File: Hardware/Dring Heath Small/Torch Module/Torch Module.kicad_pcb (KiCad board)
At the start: 2 copper layers, 86.5 x 74.7 mm, 32 parts, among them J1 Torch, J2 Module3, J3 Conn_01x18_Male, J4 Limit, J6 Motor, J7 Module1, K1 G6E, Q1 AO3400A, U1 ULN2002

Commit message: Main and Module Boards Routed
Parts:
- removed C3: 1uf, Capacitor_SMD:C_0603_1608Metric_Pad1.08x0.95mm_HandSolder
- removed R10: 3.3k, Resistor_SMD:R_0603_1608Metric_Pad0.98x0.95mm_HandSolder
- removed R8: 10k, Resistor_SMD:R_0603_1608Metric_Pad0.98x0.95mm_HandSolder
- removed R9: 1k, Resistor_SMD:R_0603_1608Metric_Pad0.98x0.95mm_HandSolder
- added J10: ~, Connector_PinHeader_2.54mm:PinHeader_1x12_P2.54mm_Vertical, F.Cu at (175.2, 129.6)
- added J8: 2.54 pin, Connector_PinHeader_2.54mm:PinHeader_2x05_P2.54mm_Vertical, F.Cu at (182.2, 111.9)
- added J9: 1.27 pin, Connector_PinHeader_1.27mm:PinHeader_2x05_P1.27mm_Vertical, F.Cu at (181.7, 125.3)
- J2: value Module3 -> ~
- J3: value Conn_01x18_Male -> ~
- moved R13 7.90 mm to (146.8, 109.1)
- moved R14 7.90 mm to (146.8, 123.6)
- moved J4 7.90 mm to (153.9, 120.3)
- moved C4 7.90 mm to (142.5, 109.1)
- moved C5 7.90 mm to (142.7, 123.6)
- moved J7 7.90 mm to (127.0, 129.7)
- moved R11 7.90 mm to (147.8, 113.9)
- moved R12 7.90 mm to (147.8, 119.0)
- moved R15 7.90 mm to (143.3, 113.9)
- moved R16 7.90 mm to (143.3, 119.0)
- moved J3 1.27 mm to (106.0, 64.3)
- moved U1 1.27 mm to (106.0, 58.4)
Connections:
- J3 pad 17: Net-(C3-Pad2) -> (no net)
- J3 pad 18: Net-(C3-Pad2) -> Net-(J3-Pad18)
- J3 pad 9: Net-(J3-Pad9) -> Net-(J3-Pad15)
- U1 pad 13: Net-(U1-Pad13) -> Net-(J3-Pad11)
- U1 pad 4: Net-(C3-Pad1) -> Net-(J3-Pad4)
- U1 pad 5: Net-(C3-Pad1) -> Net-(J3-Pad15)
- U1 pad 6: Net-(C3-Pad1) -> Net-(J3-Pad15)
- U1 pad 7: Net-(C3-Pad1) -> Net-(J3-Pad15)
- U1 pad 8: Net-(C3-Pad1) -> Net-(J3-Pad15)
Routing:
- net Net-(J3-Pad15): track 0.00 -> 50.9 mm
- net Net-(J10-Pad1): track 0.00 -> 49.9 mm
- net Net-(C3-Pad1): track 35.9 -> 0.00 mm
- net Net-(J10-Pad11): track 0.00 -> 27.1 mm
- net Net-(J10-Pad3): track 0.00 -> 26.5 mm
- net Net-(J10-Pad10): track 0.00 -> 23.4 mm, vias 0 -> 1
- net Net-(J10-Pad9): track 0.00 -> 22.3 mm, vias 0 -> 1
- net Net-(J10-Pad8): track 0.00 -> 20.5 mm
- net Net-(J3-Pad4): track 0.00 -> 15.5 mm, vias 0 -> 1
- net Net-(R10-Pad2): track 13.1 -> 0.00 mm, vias 2 -> 0
- net Net-(C3-Pad2): track 10.4 -> 0.00 mm
- net Net-(J3-Pad11): track 10.8 -> 4.35 mm, vias 1 -> 0
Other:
- board size 86.5 x 74.7 mm -> 88.6 x 79.4 mm
- board text added: "Clearpath Driver"
- board text added: "GND"
- board text added: "JTAG"
- board text added: "TCK"
- board text added: "TDI"
- board text added: "TDO"
- board text added: "TMS"
- board text added: "VCC"
- board text removed: "Z AXIS"

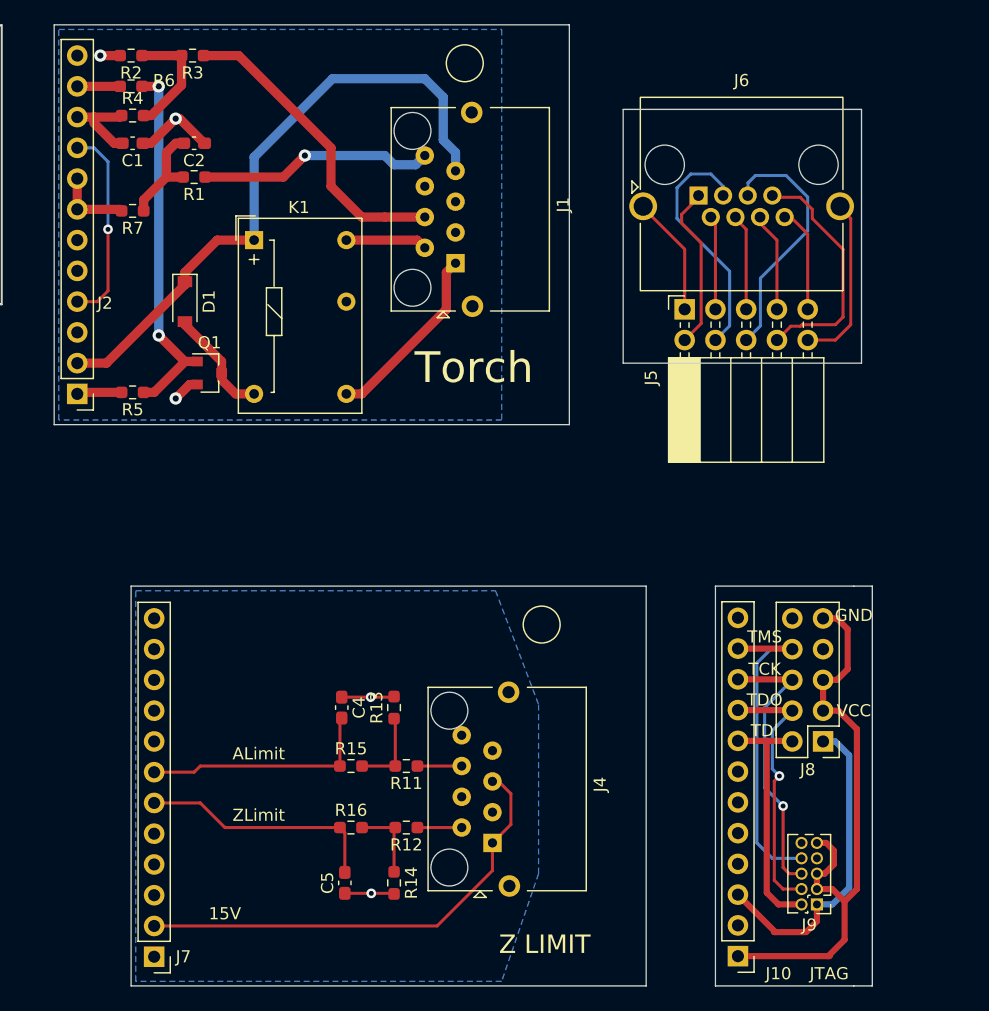
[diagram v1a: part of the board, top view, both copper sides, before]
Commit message: Pin changes
Put RJ45 connector on Jtag module for more IO put Pot on Torch module to
adjust Plasma voltage
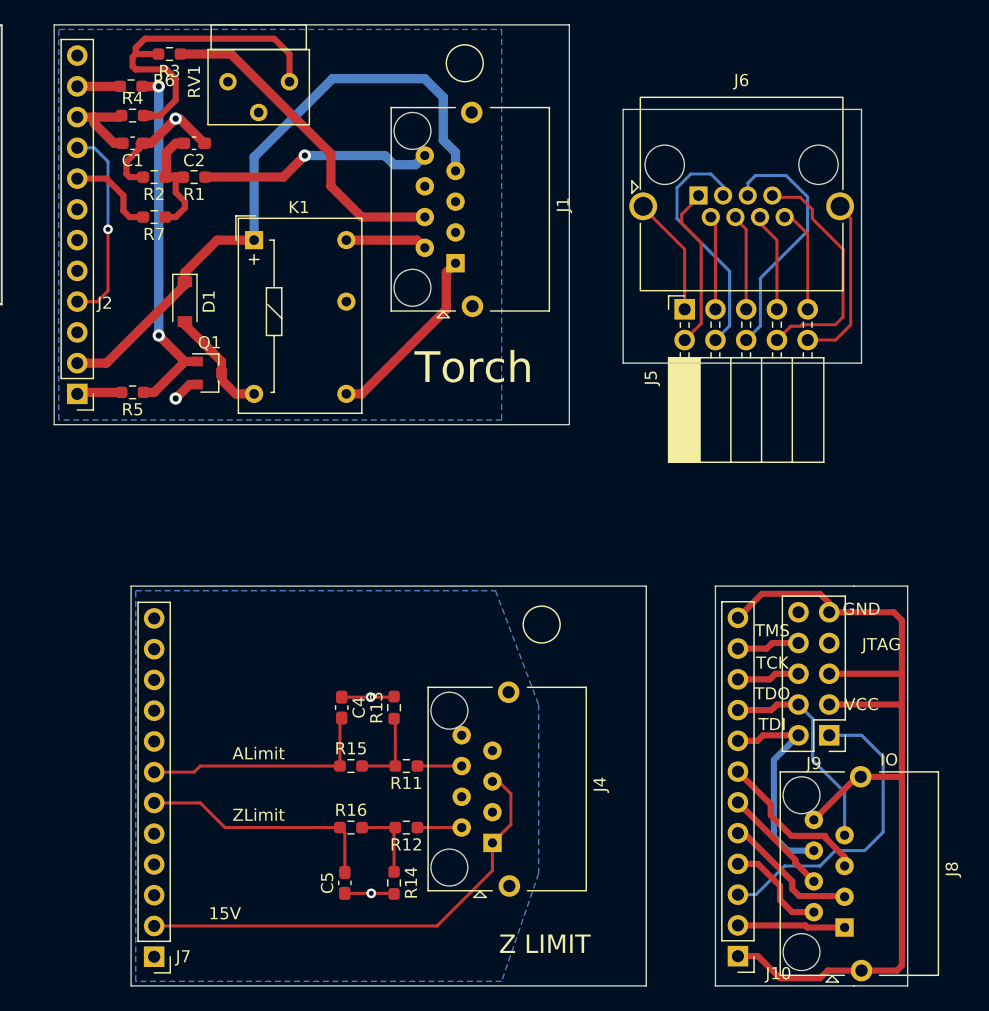
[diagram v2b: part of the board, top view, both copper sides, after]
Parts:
- added RV1: 20K, Potentiometer_THT:Potentiometer_Bourns_3339S_Horizontal, F.Cu at (133.1, 57.4)
- C2: value .1uf -> 1uf
- J2: value ~ -> Module3
- J3: value ~ -> Conn_01x18_Male
- J8: value 2.54 pin -> Torch; footprint Connector_PinHeader_2.54mm:PinHeader_2x05_P2.54mm_Vertical -> Modules:RJ45_Torb_Vertical
- J9: value 1.27 pin -> 2.54 pin; footprint Connector_PinHeader_1.27mm:PinHeader_2x05_P1.27mm_Vertical -> Connector_PinHeader_2.54mm:PinHeader_2x05_P2.54mm_Vertical
- R1: value 10k -> 3.3K
- moved J8 15.4 mm to (183.0, 127.3), turned to 90 degrees
- moved J9 14.0 mm to (182.8, 111.4)
- moved R2 10.2 mm to (127.0, 65.3)
- moved R3 1.91 mm to (128.3, 55.1)
- moved R7 1.85 mm to (127.0, 68.6)
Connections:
- J10 pad 12: Net-(J10-Pad12) -> Net-(J10-Pad1)
- J2 pad 8: Net-(J2-Pad7) -> Net-(J2-Pad8)
- J3 pad 17: (no net) -> Net-(J3-Pad17)
- J8 pad 1: Net-(J10-Pad3) -> Net-(J10-Pad2)
- J8 pad 10: Net-(J8-Pad10) -> Net-(J10-Pad1)
- J8 pad 2: Net-(J10-Pad8) -> Net-(J10-Pad4)
- J8 pad 3: Net-(J10-Pad1) -> Net-(J10-Pad5)
- J8 pad 4: Net-(J10-Pad9) -> Net-(J10-Pad6)
- J8 pad 5: Net-(J10-Pad1) -> Net-(J10-Pad7)
- J8 pad 6: Net-(J10-Pad10) -> Net-(J10-Pad8)
- J8 pad 7: Net-(J8-Pad7) -> Net-(J10-Pad9)
- J8 pad 8: Net-(J10-Pad11) -> Net-(J10-Pad1)
- R2 pad 1: Net-(R2-Pad1) -> Net-(C2-Pad2)
- R3 pad 2: Net-(R2-Pad1) -> Net-(R3-Pad2)
- R4 pad 2: Net-(R2-Pad1) -> Net-(R3-Pad2)
- R7 pad 2: Net-(J2-Pad7) -> Net-(J2-Pad8)
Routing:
- net Net-(J10-Pad1): track 49.9 -> 79.8 mm
- net Net-(R3-Pad2): track 0.00 -> 28.6 mm
- net Net-(J10-Pad11): track 27.1 -> 5.26 mm
- net Net-(J10-Pad10): track 23.4 -> 5.26 mm, vias 1 -> 0
- net Net-(J10-Pad7): track 0.00 -> 13.1 mm
- net Net-(J10-Pad5): track 0.00 -> 11.4 mm
- net Net-(R2-Pad1): track 10.8 -> 0.00 mm
- net Net-(J10-Pad6): track 0.00 -> 9.12 mm
- net Net-(J10-Pad2): track 0.00 -> 8.88 mm
- net Net-(J10-Pad4): track 0.00 -> 8.59 mm
- net Net-(J2-Pad8): track 0.00 -> 7.50 mm
- net Net-(J2-Pad7): track 6.25 -> 0.00 mm
- net Net-(J10-Pad9): track 22.3 -> 17.6 mm, vias 1 -> 0
- net Net-(C1-Pad1): track 14.4 -> 17.5 mm, vias 3 -> 2
- net Net-(J10-Pad8): track 20.5 -> 18.3 mm
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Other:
- board size 88.6 x 79.4 mm -> 91.6 x 79.4 mm
- board text added: "IO"

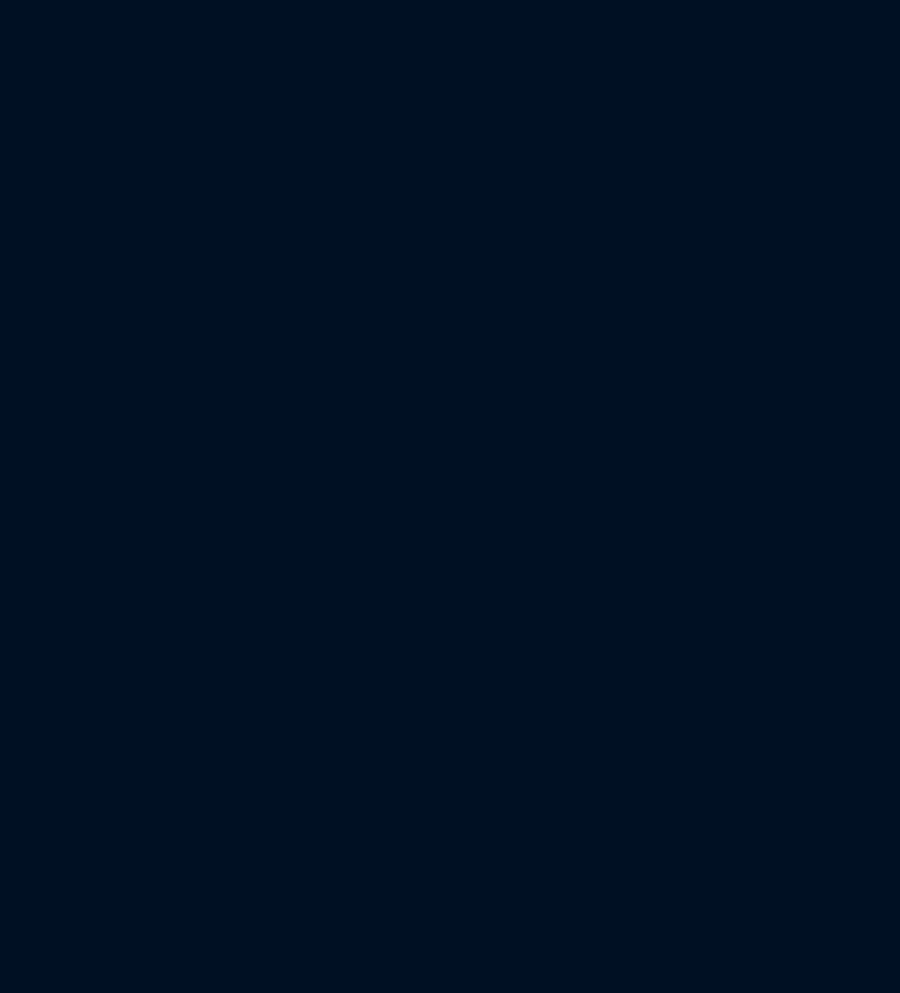
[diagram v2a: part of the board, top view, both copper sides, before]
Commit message: Added mosfet motor driver
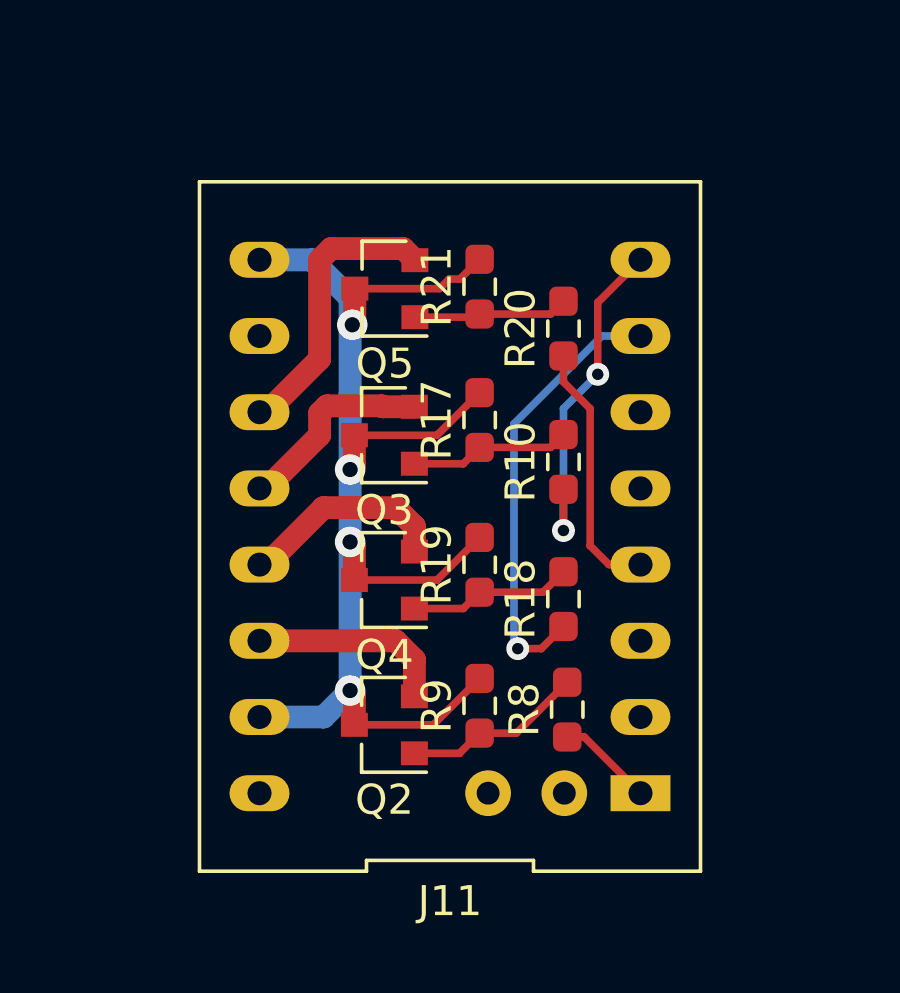
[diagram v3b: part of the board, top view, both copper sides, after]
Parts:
- added J11: Conn_01x18_Male, Modules:ClearpathDriver, F.Cu at (136.8, 150.0)
- added Q2: IRLML2402, Package_TO_SOT_SMD:SOT-23, F.Cu at (134.6, 156.6)
- added Q3: IRLML2402, Package_TO_SOT_SMD:SOT-23, F.Cu at (134.6, 146.9)
- added Q4: IRLML2402, Package_TO_SOT_SMD:SOT-23, F.Cu at (134.6, 151.8)
- added Q5: IRLML2402, Package_TO_SOT_SMD:SOT-23, F.Cu at (134.6, 142.1)
- added R10: 200, Resistor_SMD:R_0603_1608Metric_Pad0.98x0.95mm_HandSolder, F.Cu at (140.6, 147.8)
- added R17: 10k, Resistor_SMD:R_0603_1608Metric_Pad0.98x0.95mm_HandSolder, F.Cu at (137.8, 146.4)
- added R18: 200, Resistor_SMD:R_0603_1608Metric_Pad0.98x0.95mm_HandSolder, F.Cu at (140.6, 152.4)
- added R19: 10k, Resistor_SMD:R_0603_1608Metric_Pad0.98x0.95mm_HandSolder, F.Cu at (137.8, 151.3)
- added R20: 200, Resistor_SMD:R_0603_1608Metric_Pad0.98x0.95mm_HandSolder, F.Cu at (140.6, 143.4)
- added R21: 10k, Resistor_SMD:R_0603_1608Metric_Pad0.98x0.95mm_HandSolder, F.Cu at (137.8, 142.0)
- added R8: 200, Resistor_SMD:R_0603_1608Metric_Pad0.98x0.95mm_HandSolder, F.Cu at (140.7, 156.1)
- added R9: 10k, Resistor_SMD:R_0603_1608Metric_Pad0.98x0.95mm_HandSolder, F.Cu at (137.8, 156.0)
- J10: value ~ -> Module conn
- Q1: value AO3400A -> IRLML2402
- R6: value 10k -> 200
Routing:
- net Net-(J11-Pad15): track 0.00 -> 43.9 mm, vias 0 -> 4
- net Net-(J11-Pad7): track 0.00 -> 14.8 mm, vias 0 -> 1
- net Net-(J11-Pad8): track 0.00 -> 11.7 mm, vias 0 -> 2
- net Net-(J11-Pad11): track 0.00 -> 9.53 mm
- net Net-(J11-Pad4): track 0.00 -> 8.63 mm
- net Net-(J11-Pad13): track 0.00 -> 7.05 mm
- net Net-(J11-Pad12): track 0.00 -> 6.75 mm
- net Net-(J11-Pad14): track 0.00 -> 6.65 mm
- net Net-(Q2-Pad1): track 0.00 -> 6.08 mm
- net Net-(Q4-Pad1): track 0.00 -> 5.48 mm
- net Net-(Q3-Pad1): track 0.00 -> 5.37 mm
- net Net-(Q5-Pad1): track 0.00 -> 5.17 mm
- net Net-(J11-Pad1): track 0.00 -> 3.22 mm

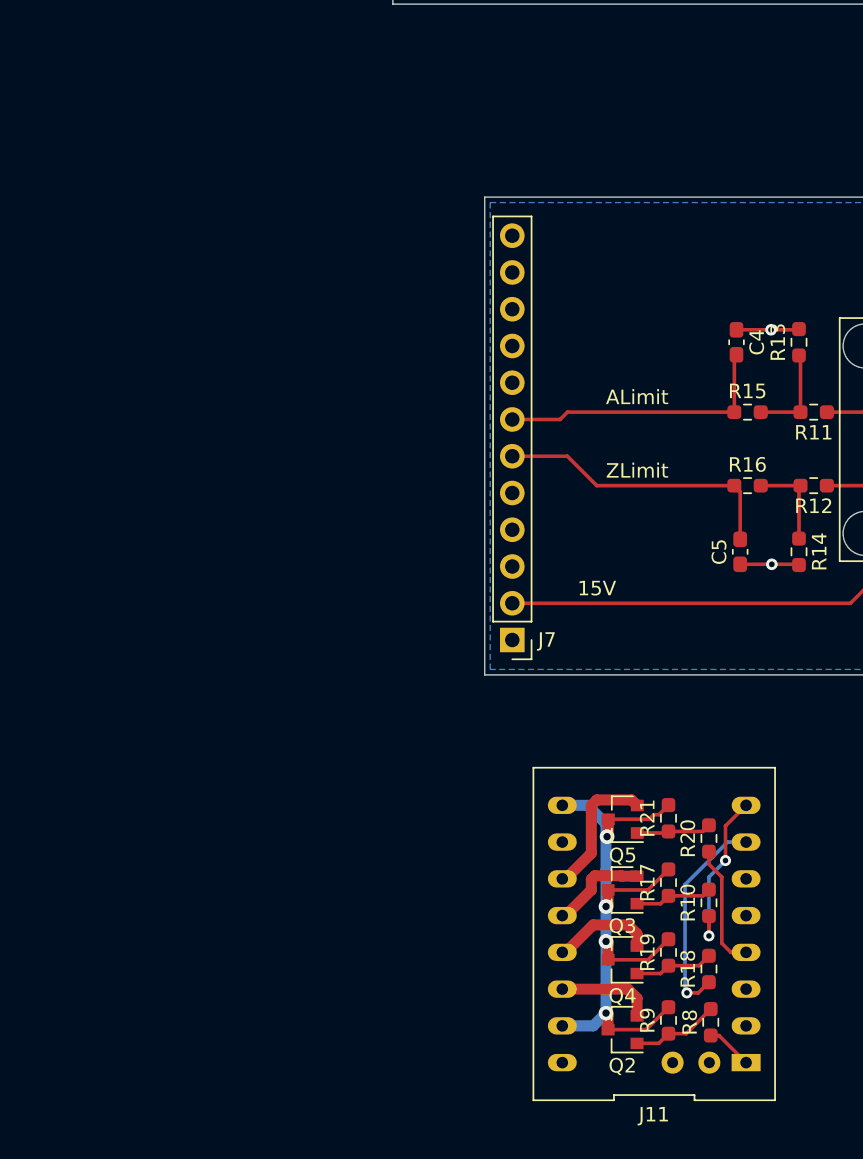
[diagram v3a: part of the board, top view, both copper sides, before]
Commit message: Changed voltage divider for THC input
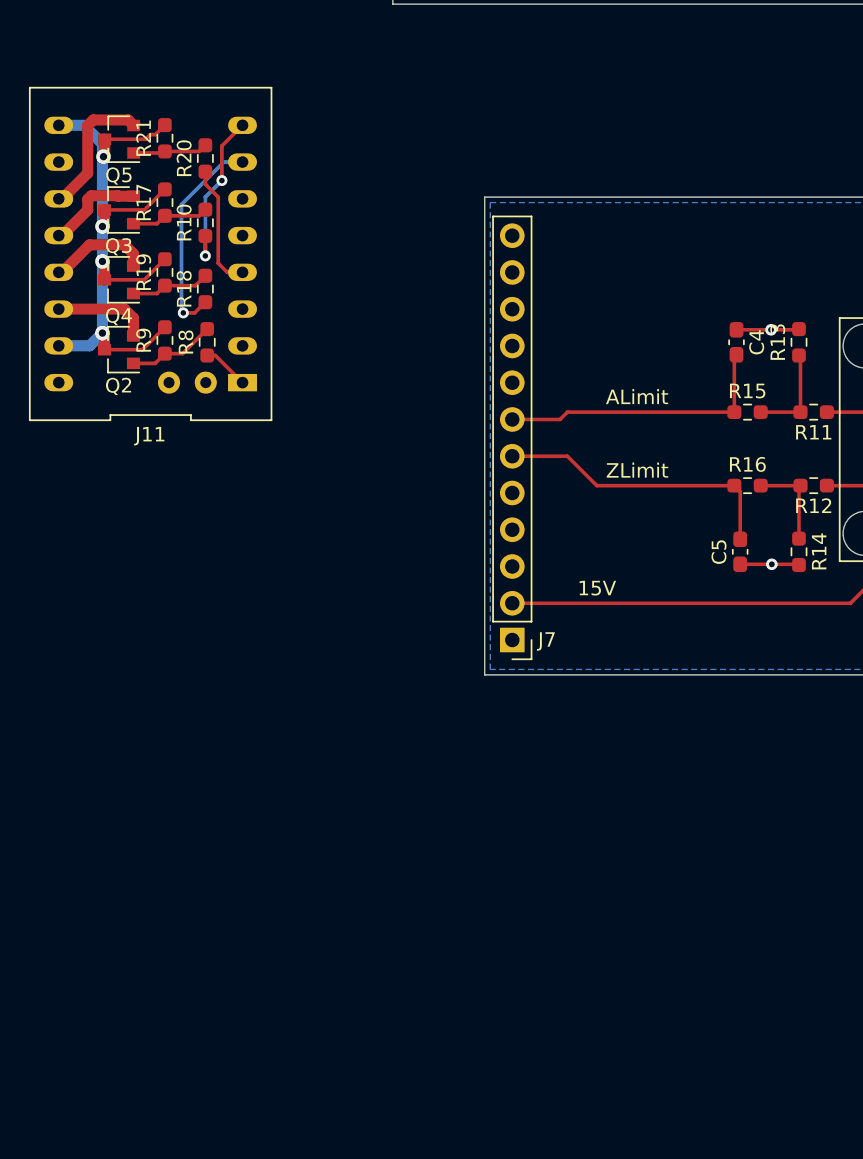
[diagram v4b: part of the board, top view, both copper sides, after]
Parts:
- C1: value 1uf -> 22nf
- R3: value 3.3k -> 1k
- RV1: value 20K -> 2K
- moved Q2 58.5 mm to (99.8, 109.6)
- moved R10 58.5 mm to (105.8, 100.8)
- moved R18 58.5 mm to (105.8, 105.4)
- moved R20 58.5 mm to (105.8, 96.4)
- moved R17 58.5 mm to (103.0, 99.4)
- moved R19 58.5 mm to (103.0, 104.3)
- moved J11 58.5 mm to (102.0, 103.0)
- moved Q3 58.5 mm to (99.8, 99.9)
- moved Q5 58.5 mm to (99.8, 95.1)
- moved R8 58.5 mm to (105.9, 109.1)
- moved Q4 58.5 mm to (99.8, 104.8)
- moved R21 58.5 mm to (103.0, 95.0)
- moved R9 58.5 mm to (103.0, 109.0)
